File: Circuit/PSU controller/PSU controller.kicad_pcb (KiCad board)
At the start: 2 copper layers, 47.6 x 32.4 mm, 13 parts, among them Q1 S8050

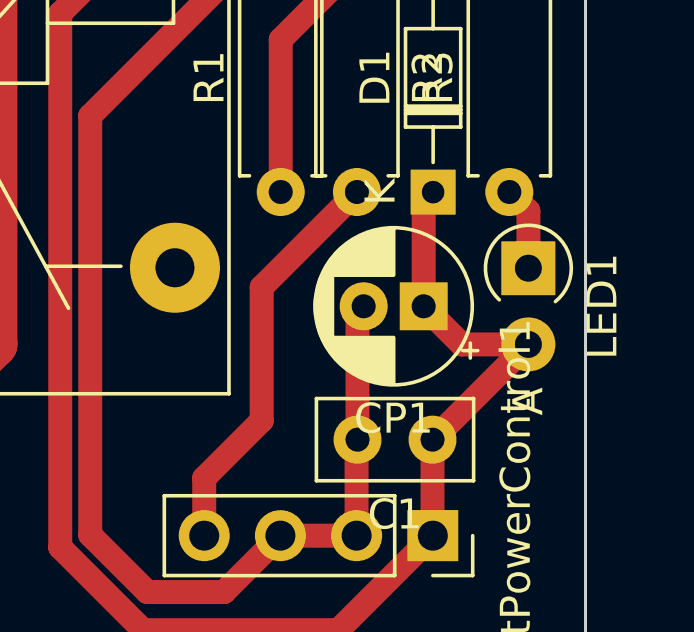
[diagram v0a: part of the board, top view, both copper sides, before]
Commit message: Modified PSU controller circuit
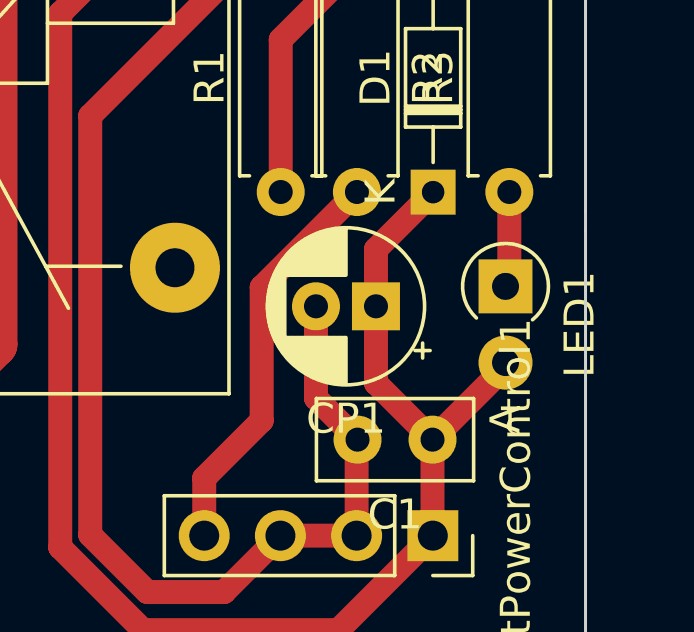
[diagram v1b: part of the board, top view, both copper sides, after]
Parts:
- moved CP1 1.59 mm to (165.1, 128.9)
- moved LED1 0.97 mm to (169.4, 128.2)
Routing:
- net +12V: track 74.8 -> 75.8 mm

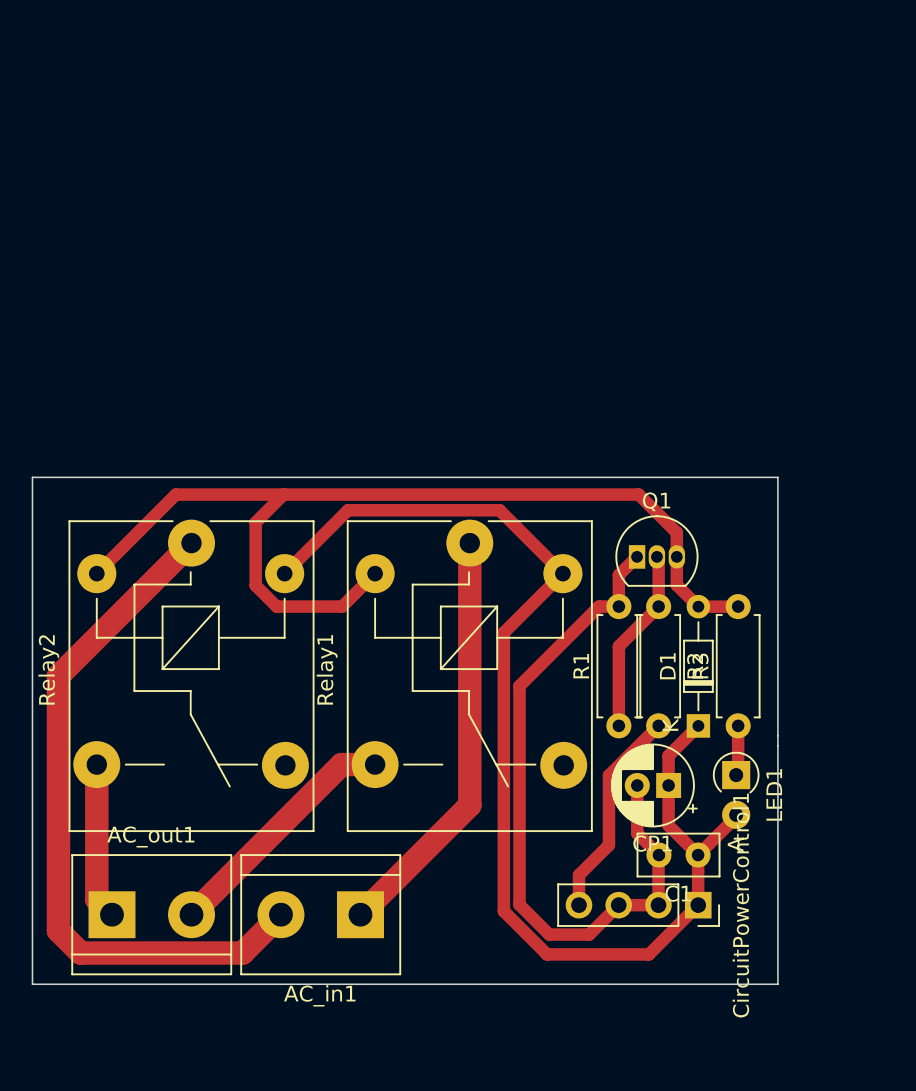
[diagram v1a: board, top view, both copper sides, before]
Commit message: Finished PCB hole CAM module
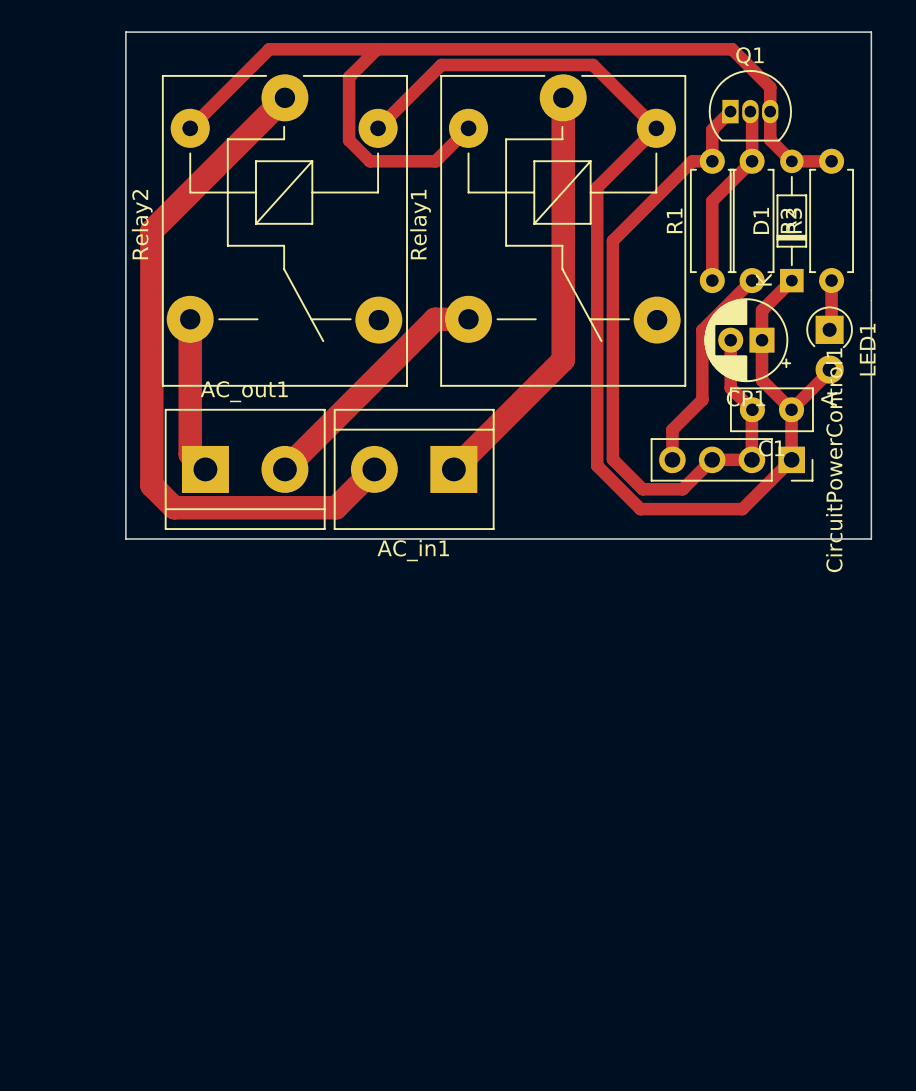
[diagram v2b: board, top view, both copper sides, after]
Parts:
- moved CP1 29.1 mm to (171.1, 100.5)
- moved CircuitPowerControl1 29.1 mm to (173.0, 108.1)
- moved LED1 29.1 mm to (175.4, 99.8)
- moved Relay1 29.1 mm to (158.4, 85.0)
- moved Relay2 29.1 mm to (140.6, 85.0)
- moved Q1 29.1 mm to (169.1, 85.9)
- moved R3 29.1 mm to (175.5, 96.6)
- moved AC_in1 29.1 mm to (151.4, 108.7)
- moved AC_out1 29.1 mm to (135.5, 108.7)
- moved C1 29.1 mm to (173.0, 104.9)
- moved D1 29.1 mm to (173.0, 96.7)
- moved R1 29.1 mm to (167.9, 96.6)
- moved R2 29.1 mm to (170.4, 89.0)

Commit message: all files updated after OS change for some reason
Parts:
- moved AC_in1 153.0 mm to (21.3, 28.2)
- moved AC_out1 153.0 mm to (5.42, 28.2)
- moved C1 153.0 mm to (42.9, 24.4)
- moved CircuitPowerControl1 153.0 mm to (42.9, 27.6)
- moved D1 153.0 mm to (42.9, 16.2)
- moved LED1 153.0 mm to (45.3, 19.3)
- moved Q1 153.0 mm to (39.0, 5.38)
- moved R1 153.0 mm to (37.8, 16.2)
- moved R2 153.0 mm to (40.3, 8.55)
- moved R3 153.0 mm to (45.4, 16.2)
- moved CP1 153.0 mm to (41.0, 20.0)
- moved Relay1 153.0 mm to (28.3, 4.50)
- moved Relay2 153.0 mm to (10.5, 4.50)

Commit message: further development in esp32-cam
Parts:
- moved AC_in1 107.3 mm to (108.8, 90.3)
- moved AC_out1 107.3 mm to (92.9, 90.3)
- moved C1 107.3 mm to (130.4, 86.5)
- moved D1 107.3 mm to (130.4, 78.3)
- moved R2 107.3 mm to (127.8, 70.7)
- moved R3 107.3 mm to (132.9, 78.3)
- moved CP1 107.3 mm to (128.5, 82.1)
- moved CircuitPowerControl1 107.3 mm to (130.4, 89.7)
- moved LED1 107.3 mm to (132.8, 81.4)
- moved Q1 107.3 mm to (126.5, 67.5)
- moved R1 107.3 mm to (125.3, 78.3)
- moved Relay1 107.3 mm to (115.8, 66.6)
- moved Relay2 107.3 mm to (98.0, 66.6)
